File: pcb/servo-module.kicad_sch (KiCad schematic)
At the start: 35 parts, among them J1 AVR-UPDI-6, J2 QWICC, J3 Power, J4 INPUT, J5 PWM1, J6 PWM2, J7 PWM3, J8 PWM4, U2 ATTINY1616MNR

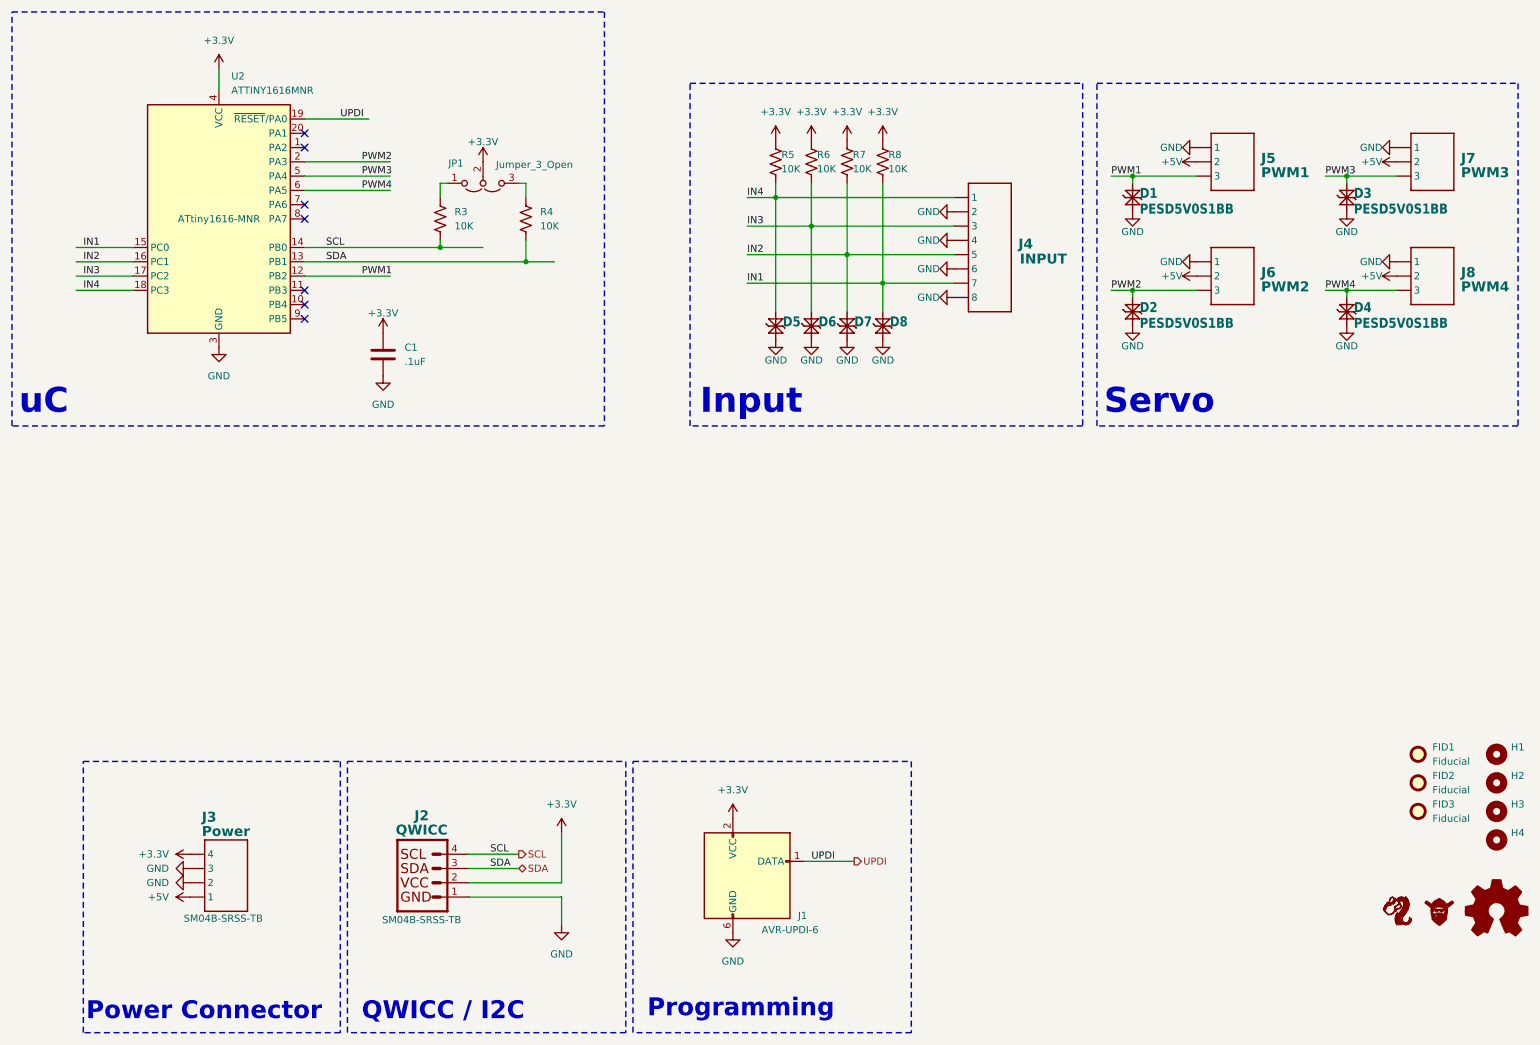
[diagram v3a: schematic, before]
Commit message: Made multi-sheet; changed LEDs to WS2812; rerouted whole board
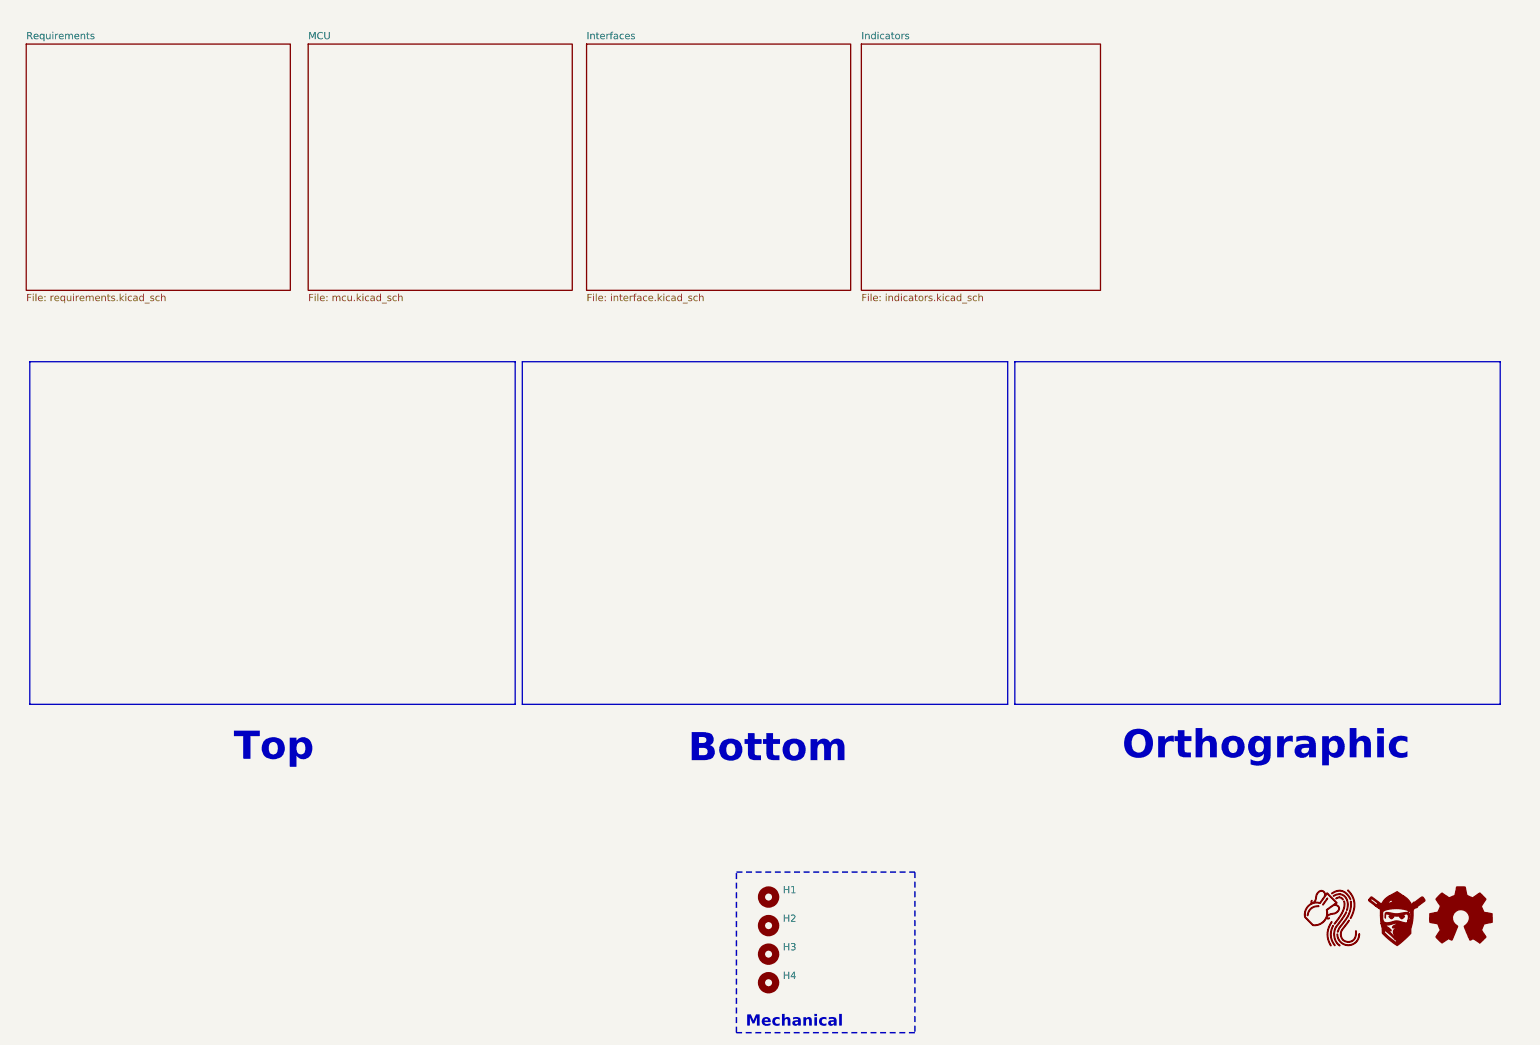
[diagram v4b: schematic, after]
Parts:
- removed C1: .1uF, Capacitor_SMD:C_0603_1608Metric, symbol Device:C
- removed D1, D2, D3, D4, D5, D6, D7, D8: PESD5V0S1BB, CRGM Passive:D_SOD-523, symbol CRGM Passive:PESD5V0S1BB
- removed FID1, FID2, FID3: Fiducial, Fiducial:Fiducial_0.75mm_Mask1.5mm, symbol Mechanical:Fiducial
- removed J1: AVR-UPDI-6, Connector_PinHeader_2.54mm:PinHeader_2x03_P2.54mm_Vertical, symbol Connector:AVR-UPDI-6
- removed J2: QWICC, Connector_JST:JST_SH_SM04B-SRSS-TB_1x04-1MP_P1.00mm_Horizontal, symbol CRGM Connector:QWIIC
- removed J3: Power, Connector_JST:JST_SH_SM04B-SRSS-TB_1x04-1MP_P1.00mm_Horizontal, symbol CRGM Connector:JST-SH-4
- removed J4: INPUT, Connector_JST:JST_SH_BM08B-SRSS-TB_1x08-1MP_P1.00mm_Vertical, symbol CRGM Connector:JST-SH-8
- removed J5: PWM1, Connector_JST:JST_SH_BM03B-SRSS-TB_1x03-1MP_P1.00mm_Vertical, symbol CRGM Connector:JST-SH-3
- removed J6: PWM2, Connector_JST:JST_SH_BM03B-SRSS-TB_1x03-1MP_P1.00mm_Vertical, symbol CRGM Connector:JST-SH-3
- removed J7: PWM3, Connector_JST:JST_SH_BM03B-SRSS-TB_1x03-1MP_P1.00mm_Vertical, symbol CRGM Connector:JST-SH-3
- removed J8: PWM4, Connector_JST:JST_SH_BM03B-SRSS-TB_1x03-1MP_P1.00mm_Vertical, symbol CRGM Connector:JST-SH-3
- removed JP1: Jumper_3_Open, Jumper:SolderJumper-3_P1.3mm_Open_RoundedPad1.0x1.5mm_NumberLabels, symbol Jumper:Jumper_3_Open
- removed R3, R4, R5, R6, R7, R8: 10K, Resistor_SMD:R_0603_1608Metric, symbol Device:R_US
- removed U2: ATTINY1616MNR, Package_DFN_QFN:VQFN-20-1EP_3x3mm_P0.4mm_EP1.7x1.7mm, symbol MCU_Microchip_ATtiny:ATtiny1616-M
- LOGO1: footprint CRGM Logos:Aquarius Logo 10mm -> CRGM Logos:Aquarius Logo 8mm
- LOGO2: renamed from LOGO3; footprint CRGM Logos:FNWW Face 10mm -> CRGM Logos:FNWW Face 8mm
- renumbered LOGO5 to LOGO3
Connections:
- no-connect marks 7 -> 0
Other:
- added sheet Indicators (indicators.kicad_sch)
- added sheet Interfaces (interface.kicad_sch)
- added sheet MCU (mcu.kicad_sch)
- added sheet Requirements (requirements.kicad_sch)
- note added: "Bottom"
- note added: "Mechanical"
- note added: "Orthographic"
- note added: "Top"
- note removed: "Input"
- note removed: "Power Connector"
- note removed: "Programming"
- note removed: "QWICC / I2C"
- note removed: "Servo"
- note removed: "uC"
- moved on the sheet: H1, H2, H3, H4

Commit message: Updated frame template
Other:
- company: CRG Makes -> (none)
